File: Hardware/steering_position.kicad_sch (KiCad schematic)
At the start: 5 parts, among them U19 MCP6001-OT

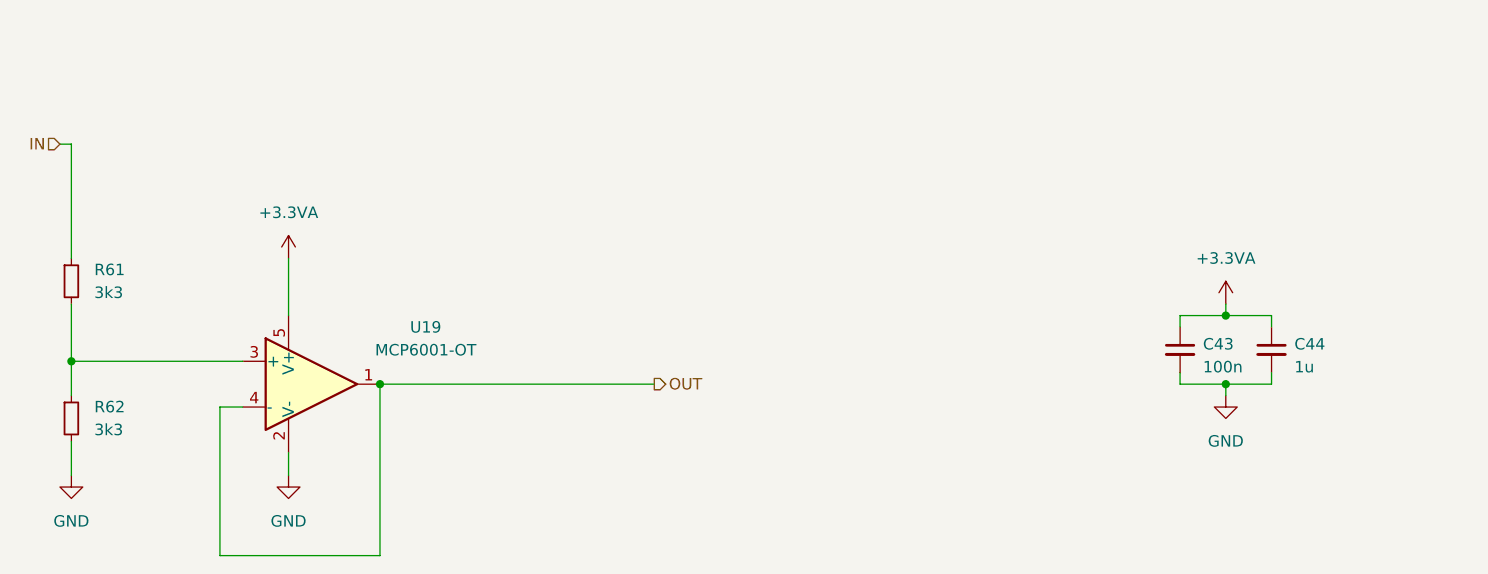
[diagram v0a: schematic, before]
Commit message: Changes in current layout, added tensometers to layout
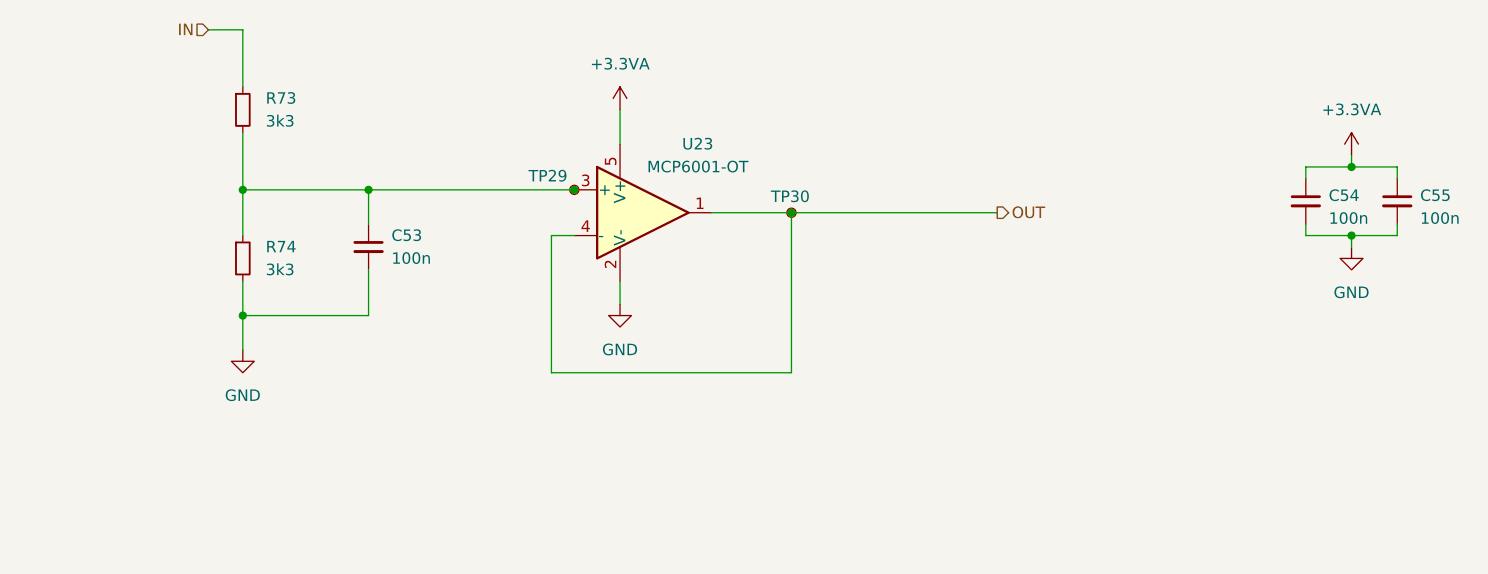
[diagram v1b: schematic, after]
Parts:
- removed C43: 100n, Capacitor_SMD:C_0603_1608Metric, symbol Device:C_Small
- removed C44: 1u, Capacitor_SMD:C_0402_1005Metric_Pad0.74x0.62mm_HandSolder, symbol Device:C_Small
- removed R61, R62: 3k3, Resistor_SMD:R_0402_1005Metric_Pad0.72x0.64mm_HandSolder, symbol Device:R_Small
- removed U19: MCP6001-OT, Package_TO_SOT_SMD:SOT-23-5, symbol Amplifier_Operational:MCP6001-OT
- added C53, C54, C55: 100n, Capacitor_SMD:C_0603_1608Metric, symbol Device:C_Small
- added R73, R74: 3k3, Resistor_SMD:R_0603_1608Metric, symbol Device:R_Small
- added TP29, TP30: TestPoint_Small, TestPoint:TestPoint_Pad_D1.0mm, symbol Connector:TestPoint_Small
- added U23: MCP6001-OT, Package_TO_SOT_SMD:SOT-23-5, symbol Amplifier_Operational:MCP6001-OT
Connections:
- net +3.3VA: now also C54.1, C55.1, U23.5 (V+)
- net GND: now also C53.2, C54.2, C55.2, R74.2, U23.2 (V-)
- net IN: now also R73.1
- net OUT: now also TP30.1, U23.1, U23.4 (-)
- new net: C53.1, R73.2, R74.1, TP29.1, U23.3 (+)
